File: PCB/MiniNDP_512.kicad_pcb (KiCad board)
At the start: 2 copper layers, 60 x 34 mm, 23 parts, among them J1 Conn_02x20_Odd_Even, U1 HC161, U2 HC161, U3 HC161, U4 HC138, U5 HC374, U6 AS6C4008, U7 1G32, U8 1G79

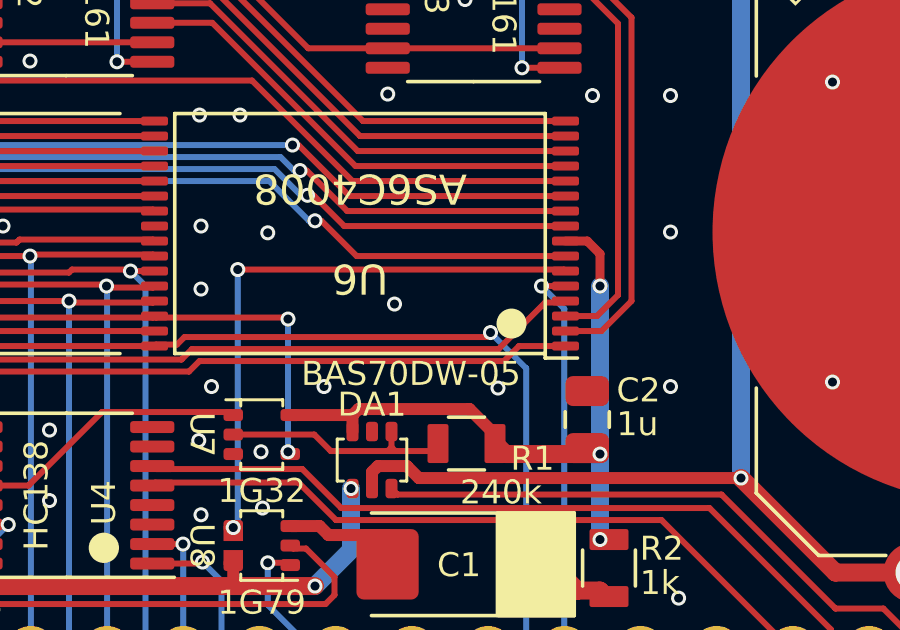
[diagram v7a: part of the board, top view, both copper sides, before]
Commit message: remove redundant user.dwg
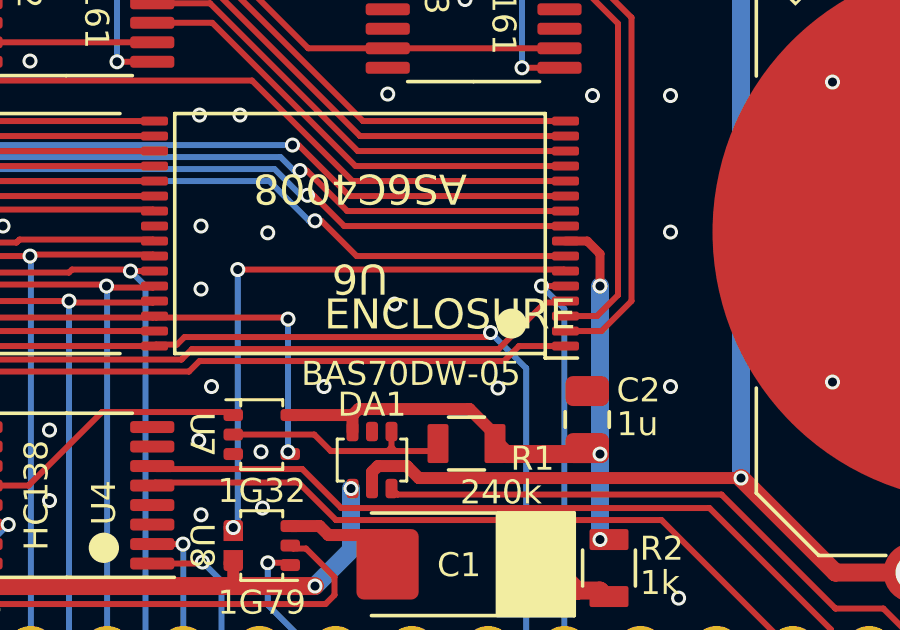
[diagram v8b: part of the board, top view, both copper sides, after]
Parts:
- added ENCLOSURE: MiniNDP_Cover, 000_LOCAL:MiniNDP_Cover, F.Cu at (151.9, 103.0)
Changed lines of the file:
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@@
 		)
 	)
+	(footprint "000_LOCAL:MiniNDP_Cover"
+		(layer "F.Cu")
+		(at 151.95 103.025)
+		(property "Reference" "ENCLOSURE"
+			(at 0 -0.5 0)
+			(unlocked yes)
+			(layer "F.SilkS")
+			(effects
+				(font
+					(size 1 1)
+					(thickness 0.15)
+				)
+			)
+		)
+		(property "Value" "MiniNDP_Cover"
+			(at 0 1 0)
+			(unlocked yes)
+			(layer "F.Fab")
+			(effects
+				(font
+					(size 1 1)
+					(thickness 0.15)
+				)
+			)
+		)
+		(property "Footprint" "000_LOCAL:MiniNDP_Cover"
+			(at 0 0 0)
+			(unlocked yes)
+			(layer "F.Fab")
+			(hide yes)
+			(effects
+				(font
+					(size 1 1)
+					(thickness 0.15)
+				)
+			)
+		)
+		(property "Datasheet" ""
+			(at 0 0 0)
+			(unlocked yes)
+			(layer "F.Fab")
+			(hide yes)
+			(effects
+				(font
+					(size 1 1)
+					(thickness 0.15)
+				)
+			)
+		)
+		(property "Description" ""
+			(at 0 0 0)
+			(unlocked yes)
+			(layer "F.Fab")
+			(hide yes)
+			(effects
+				(font
+					(size 1 1)
+					(thickness 0.15)
+				)
+			)
+		)
+		(attr board_only exclude_from_pos_files exclude_from_bom allow_missing_courtyard)
+		(fp_line
+			(start -29.2 -15)
+			(end -29.2 15)
+			(stroke
+				(width 0.02)
+				(type default)
+			)
+			(layer "Dwgs.User")
+		)
+		(fp_line
+			(start -28 -16.2)
+			(end 28 -16.2)
+			(stroke
+				(width 0.02)
+				(type default)
+			)
+			(layer "Dwgs.User")
+		)
+		(fp_line
+			(start -28 16.2)
+			(end 28 16.2)
+			(stroke
+				(width 0.02)
+				(type default)
+			)
+			(layer "Dwgs.User")
+		)
+		(fp_line
+			(start 29.2 -15)
+			(end 29.2 15)
+			(stroke
+				(width 0.02)
+				(type default)
+			)
+			(layer "Dwgs.User")
+		)
+		(fp_arc
+			(start -29.2 -15)
+			(mid -28.848528 -15.848528)
+			(end -28 -16.2)
+			(stroke
+				(width 0.02)
+				(type default)
+			)
+			(layer "Dwgs.User")
+		)
+		(fp_arc
+			(start -28 16.2)
+			(mid -28.848528 15.848528)
+			(end -29.2 15)
+			(stroke
+				(width 0.02)
+				(type default)
+			)
+			(layer "Dwgs.User")
+		)
+		(fp_arc
+			(start 28 -16.2)
+			(mid 28.848528 -15.848528)
+			(end 29.2 -15)
+			(stroke
+				(width 0.02)
+				(type default)
+			)
+			(layer "Dwgs.User")
+		)
+		(fp_arc
+			(start 29.2 15)
+			(mid 28.848528 15.848528)
+			(end 28 16.2)
+			(stroke
+				(width 0.02)
+				(type default)
+			)
+			(layer "Dwgs.User")
+		)
+		(group ""
+			(members "35439be9-08e1-4840-96df-1bbb7dd26791" "3e1f6ce2-1ea8-4b77-b794-24120dbaa0ba"
+				"619f22c4-69a6-47ea-bb64-ae0e9f0736d0" "65834d9e-5d2e-421e-aa74-81786d07fc86"
+				"9bb228dc-0308-4114-84e6-46a9436f4e4c" "9bd79061-17d1-4628-829d-3de83d2c22c6"
+				"b11e9b62-bcf3-4a8c-a0c7-8f393ade95ab" "e0c22c64-d8a7-47b9-9dab-4a1a083193fc"
+			)
+		)
+		(model "${KIPRJMOD}/000_LOCAL.pretty/3dshapes/MiniNDP_Cover.step"
+			(hide yes)
+			(offset
+				(xyz 0 0 -1.6)
+			)
+			(scale
+				(xyz 1 1 1)
+			)
+			(rotate
+				(xyz 0 0 0)
+			)
+		)
+		(model "${KIPRJMOD}/000_LOCAL.pretty/3dshapes/MiniNDP_Cover_t.step"
+			(offset
+				(xyz 0 0 -1.6)
+			)
+			(scale
+				(xyz 1 1 1)
+			)
+			(rotate
+				(xyz 0 0 0)
+			)
+		)
+	)
 	(footprint "000_LOCAL:C_0805"
 		(layer "F.Cu")
@@
 	)
 	(gr_line
-		(start 123.95 119.225)
-		(end 179.95 119.225)
-		(stroke
-			(width 0.02)
-			(type default)
-		)
-		(layer "Dwgs.User")
-	)
-	(gr_arc
-		(start 122.75 88.025)
-		(mid 123.101472 87.176472)
-		(end 123.95 86.825)
-		(stroke
-			(width 0.02)
-			(type default)
-		)
-		(layer "Dwgs.User")
-	)
-	(gr_line
 		(start 154.45 119.1)
 		(end 154.25 118.9)
@@
 	)
 	(gr_line
-		(start 122.75 88.025)
-		(end 122.75 118.025)
-		(stroke
-			(width 0.02)
-			(type default)
-		)
-		(layer "Dwgs.User")
-	)
-	(gr_arc
-		(start 123.95 119.225)
-		(mid 123.101472 118.873528)
-		(end 122.75 118.025)
-		(stroke
-			(width 0.02)
-			(type default)
-		)
-		(layer "Dwgs.User")
-	)
-	(gr_arc
-		(start 179.95 86.825)
-		(mid 180.798528 87.176472)
-		(end 181.15 88.025)
-		(stroke
-			(width 0.02)
-			(type default)
-		)
-		(layer "Dwgs.User")
-	)
-	(gr_line
-		(start 123.95 86.825)
-		(end 179.95 86.825)
-		(stroke
-			(width 0.02)
-			(type default)
-		)
-		(layer "Dwgs.User")
-	)
-	(gr_line
-		(start 181.15 88.025)
-		(end 181.15 118.025)
-		(stroke
-			(width 0.02)
-			(type default)
-		)
-		(layer "Dwgs.User")
-	)
-	(gr_arc
-		(start 181.15 118.025)
-		(mid 180.798528 118.873528)
-		(end 179.95 119.225)
-		(stroke
-			(width 0.02)
-			(type default)
-		)
-		(layer "Dwgs.User")
-	)
-	(gr_line
 		(start 154.45 119.1)
 		(end 154.65 118.9)
@@
 		)
 	)
-	(group ""
-		(members "2377220b-e04d-4b81-ac5a-a1b9f679845b" "293695ee-931b-4bc5-802d-b60be26dd645"
-			"3cec5b49-d6fa-4a27-8fc8-465a14676a6e" "3e78ce8d-5c23-4b43-bf3c-0a43a453ad55"
-			"444327b1-bdaa-4f00-8a88-f7abaaed7b07" "4880f06d-8220-493e-81e7-b1eaa7b5cd00"
-			"654ecf28-9388-4528-9a5e-542e15eab4d2" "c91c7ba7-5c10-43f0-8d03-23363b4ac31e"
-		)
-	)
